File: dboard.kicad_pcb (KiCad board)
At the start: 2 copper layers, 44.7 x 8.7 mm, 10 parts, among them J1 USB_C_Receptacle_USB2.0, J2 Conn_01x04_MountingPin

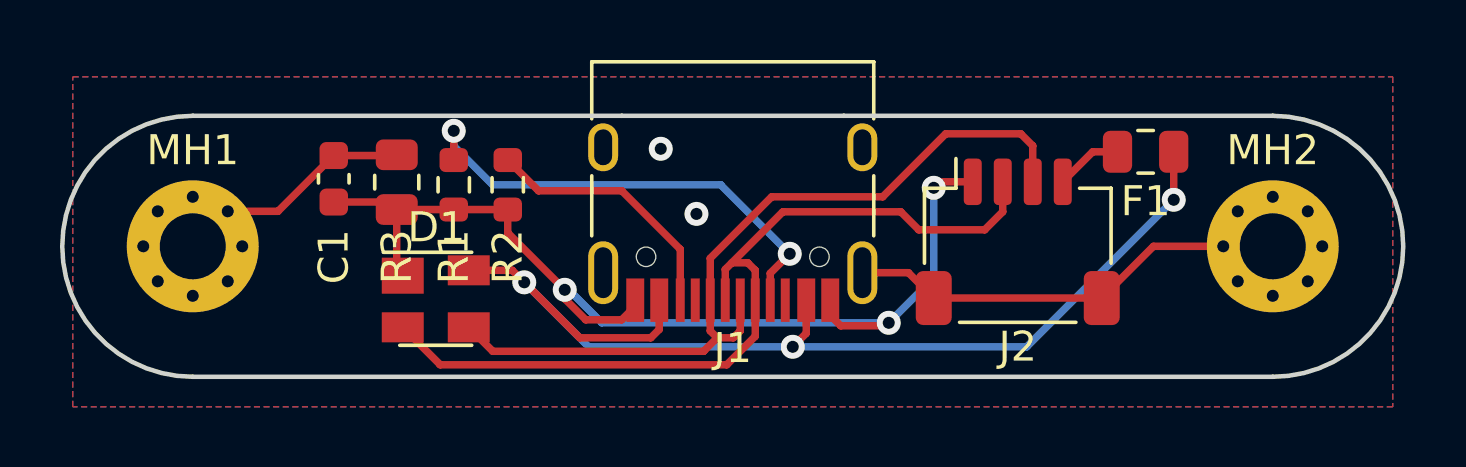
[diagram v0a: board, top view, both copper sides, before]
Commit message: fixed pinout
made pinout udb compatible
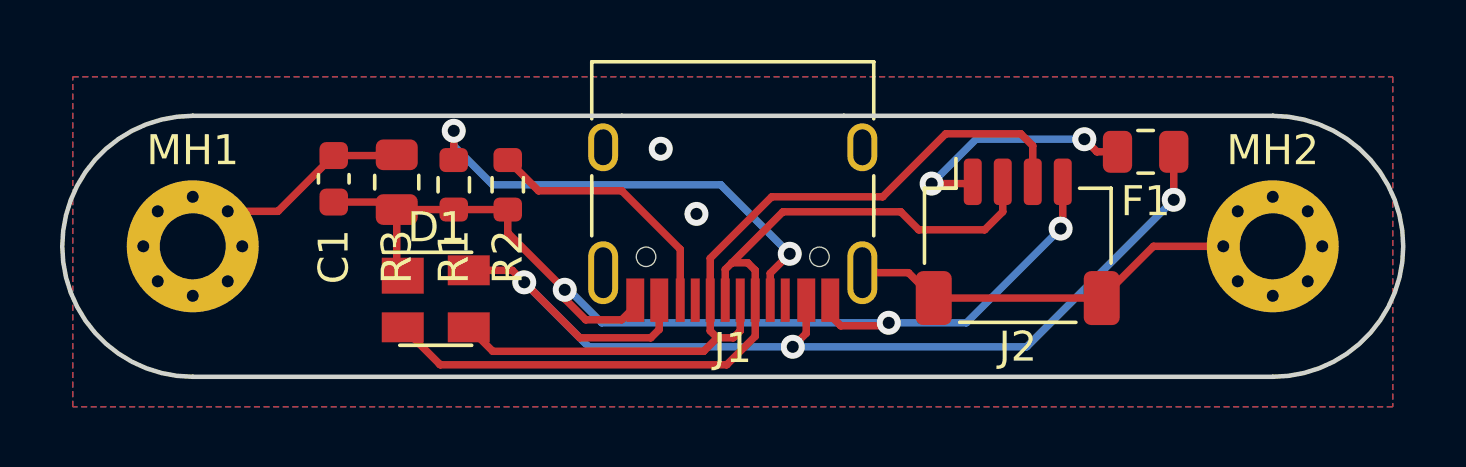
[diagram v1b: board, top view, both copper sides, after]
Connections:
- J2 pad 1: GND -> +5V
- J2 pad 4: +5V -> GND
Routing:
- net +5V: track 2.24 -> 8.38 mm, vias 0 -> 2
- net GND: track 35.4 -> 37.5 mm
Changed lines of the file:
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@@
     (fp_line (start -3 2.575) (end 3 2.575) (layer "F.Fab") (width 0.1))
     (pad "1" smd roundrect locked (at -1.5 -2) (size 0.6 1.55) (layers "F.Cu" "F.Paste" "F.Mask") (roundrect_rratio 0.25)
-      (net 2 "GND") (pinfunction "Pin_1") (pintype "passive"))
+      (net 6 "+5V") (pinfunction "Pin_1") (pintype "passive"))
     (pad "2" smd roundrect locked (at -0.5 -2) (size 0.6 1.55) (layers "F.Cu" "F.Paste" "F.Mask") (roundrect_rratio 0.25)
       (net 3 "D-") (pinfunction "Pin_2") (pintype "passive"))
@@
       (net 1 "D+") (pinfunction "Pin_3") (pintype "passive"))
     (pad "4" smd roundrect locked (at 1.5 -2) (size 0.6 1.55) (layers "F.Cu" "F.Paste" "F.Mask") (roundrect_rratio 0.25)
-      (net 6 "+5V") (pinfunction "Pin_4") (pintype "passive"))
+      (net 2 "GND") (pinfunction "Pin_4") (pintype "passive"))
     (pad "MP" smd roundrect locked (at -2.8 1.875) (size 1.2 1.8) (layers "F.Cu" "F.Paste" "F.Mask") (roundrect_rratio 0.2083333333)
       (net 5 "SHIELD") (pinfunction "MountPin") (pintype "passive"))
@@
     (effects (font (size 1 1) (thickness 0.15) italic) (justify mirror))
   )
+  (dimension (type aligned) (layer "B.Cu")
+    (pts (xy 0 -0.25) (xy 0 10))
+    (height -29.36875)
+    (gr_text "10,2500 mm" (at 27.56875 4.875 90) (layer "B.Cu")
+      (effects (font (size 1.5 1.5) (thickness 0.3)))
+    )
+    (format (units 3) (units_format 1) (precision 4))
+    (style (thickness 0.12) (arrow_length 1.27) (text_position_mode 0) (extension_height 0.58642) (extension_offset 0.5) keep_text_aligned)
+  )
   (dimension (type aligned) (layer "Eco1.User")
     (pts (xy 22.4 5.6) (xy -22.4 5.6))
@@
   (segment (start 10 2.3) (end 9.6 1.9) (width 0.25) (layer "F.Cu") (net 1))
   (segment (start -0.75 8.469022) (end -0.519022 8.7) (width 0.25) (layer "F.Cu") (net 1))
-  (segment (start 6.9 3.5) (end 6.7 3.7) (width 0.25) (layer "F.Cu") (net 2))
   (segment (start -7.5 5.2) (end -5.6 7.1) (width 0.25) (layer "F.Cu") (net 2))
   (segment (start -11.45 4.175) (end -11.2 4.425) (width 0.25) (layer "F.Cu") (net 2))
   (segment (start -7.5 4.425) (end -7.5 5.2) (width 0.25) (layer "F.Cu") (net 2))
   (segment (start 3.6 8.3) (end 5.1 8.3) (width 0.25) (layer "F.Cu") (net 2))
-  (segment (start 8 3.5) (end 6.9 3.5) (width 0.25) (layer "F.Cu") (net 2))
   (segment (start 5.1 8.3) (end 5.2 8.2) (width 0.25) (layer "F.Cu") (net 2))
   (segment (start -11.2 6.43) (end -11 6.63) (width 0.25) (layer "F.Cu") (net 2))
   (segment (start -3.7 8.1) (end -4.9 8.1) (width 0.25) (layer "F.Cu") (net 2))
   (segment (start 3.25 7.95) (end 3.6 8.3) (width 0.25) (layer "F.Cu") (net 2))
+  (segment (start 11 3.5) (end 11 4.99) (width 0.25) (layer "F.Cu") (net 2))
   (segment (start -13.3 4.175) (end -11.45 4.175) (width 0.25) (layer "F.Cu") (net 2))
+  (segment (start 11 4.99) (end 10.93 5.06) (width 0.25) (layer "F.Cu") (net 2))
   (segment (start -3.25 7.65) (end -3.7 8.1) (width 0.25) (layer "F.Cu") (net 2))
   (segment (start -7.5 4.425) (end -9.3 4.425) (width 0.25) (layer "F.Cu") (net 2))
@@
   (segment (start -11.2 4.425) (end -11.2 6.43) (width 0.25) (layer "F.Cu") (net 2))
   (via (at 5.2 8.2) (size 0.8) (drill 0.4) (layers "F.Cu" "B.Cu") (net 2))
-  (via (at 6.7 3.7) (size 0.8) (drill 0.4) (layers "F.Cu" "B.Cu") (net 2))
+  (via (at 10.93 5.06) (size 0.8) (drill 0.4) (layers "F.Cu" "B.Cu") (net 2))
   (via (at -5.6 7.1) (size 0.8) (drill 0.4) (layers "F.Cu" "B.Cu") (net 2))
+  (segment (start 5.2 8.2) (end 7.79 8.2) (width 0.25) (layer "B.Cu") (net 2))
   (segment (start -5.466047 7.1) (end -5.6 7.1) (width 0.25) (layer "B.Cu") (net 2))
-  (segment (start 6.7 3.7) (end 6.7 6.7) (width 0.25) (layer "B.Cu") (net 2))
+  (segment (start 7.79 8.2) (end 10.93 5.06) (width 0.25) (layer "B.Cu") (net 2))
   (segment (start 5.2 8.2) (end -4.366047 8.2) (width 0.25) (layer "B.Cu") (net 2))
-  (segment (start 6.7 6.7) (end 5.2 8.2) (width 0.25) (layer "B.Cu") (net 2))
   (segment (start -4.366047 8.2) (end -5.466047 7.1) (width 0.25) (layer "B.Cu") (net 2))
   (segment (start -0.2 9.6) (end -9.75 9.6) (width 0.25) (layer "F.Cu") (net 3))
@@
   (via (at -2.4 2.4) (size 0.8) (drill 0.4) (layers "F.Cu" "B.Cu") (free) (net 5))
   (via (at -1.21 4.57) (size 0.8) (drill 0.4) (layers "F.Cu" "B.Cu") (free) (net 5))
-  (segment (start 12 2.5) (end 11 3.5) (width 0.25) (layer "F.Cu") (net 6))
-  (segment (start 12.825 2.5) (end 12 2.5) (width 0.25) (layer "F.Cu") (net 6))
+  (segment (start 12.14 2.5) (end 11.72 2.08) (width 0.25) (layer "F.Cu") (net 6))
+  (segment (start 7.94 3.56) (end 8 3.5) (width 0.25) (layer "F.Cu") (net 6))
+  (segment (start 12.825 2.5) (end 12.14 2.5) (width 0.25) (layer "F.Cu") (net 6))
+  (segment (start 6.63 3.56) (end 7.94 3.56) (width 0.25) (layer "F.Cu") (net 6))
+  (via (at 6.63 3.56) (size 0.8) (drill 0.4) (layers "F.Cu" "B.Cu") (net 6))
+  (via (at 11.72 2.08) (size 0.8) (drill 0.4) (layers "F.Cu" "B.Cu") (net 6))
+  (segment (start 11.72 2.08) (end 8.11 2.08) (width 0.25) (layer "B.Cu") (net 6))
+  (segment (start 8.11 2.08) (end 6.63 3.56) (width 0.25) (layer "B.Cu") (net 6))
   (segment (start 1.25 7.445) (end 1.25 6.55) (width 0.25) (layer "F.Cu") (net 7))
   (segment (start 1.25 6.55) (end 1.9 5.9) (width 0.25) (layer "F.Cu") (net 7))
